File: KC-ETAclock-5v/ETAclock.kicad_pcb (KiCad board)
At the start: 2 copper layers, 240 x 38.7 mm, 125 parts, among them J1 Conn_01x01, J2 Conn_01x01, J3 Conn_01x01, J4 Conn_01x01, J5 USB_SUPPLY, J6 Conn_01x05, P15 Raspberry_PI_Zero_Hat, Q10 MMBTA42, Q11 MMBTA92, Q12 MMBTA42, Q13 MMBTA92, Q14 MMBTA42, Q15 MMBTA92, Q16 MMBTA42, Q17 MMBTA92, Q18 MMBTA42, Q19 MMBTA92, Q2 MMBTA42, Q20 MMBTA42, Q21 MMBTA92, Q22 MMBTA42, Q23 MMBTA92, Q24 MMBTA42, Q25 MMBTA92, Q3 MMBTA92, Q4 MMBTA42, Q5 MMBTA92, Q6 MMBTA42, Q7 MMBTA92, Q8 MMBTA42, Q9 MMBTA92, U10 IN-4, U11 TPIC6B595, U12 IN-4, U13 IN-4, U14 TPIC6B595, U3 IN-4, U4 TPIC6B595, U5 IN-4, U6 74HCT04, U7 TPIC6B595, U8 IN-4, U9 TPIC6B595

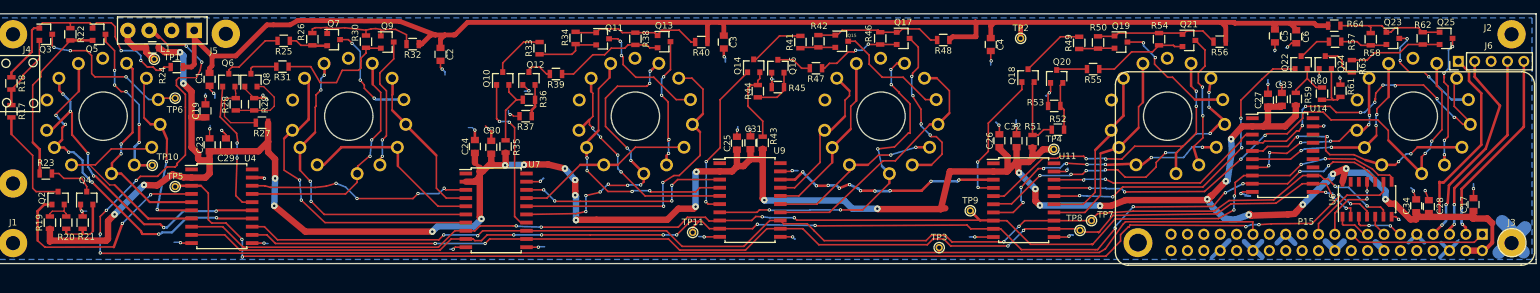
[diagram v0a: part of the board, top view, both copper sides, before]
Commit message: New V2 of Layout to Fix Nixie Tube radius offset and the Nixie tube pin 3 placement.   It is suppose to be at 49 degree C instead of 43 degree c.
Code was updated to add Fade In and Fade Out commands.  Also Code updated to
Add an option for a PIR sensor. The PIR Sensor code is working.
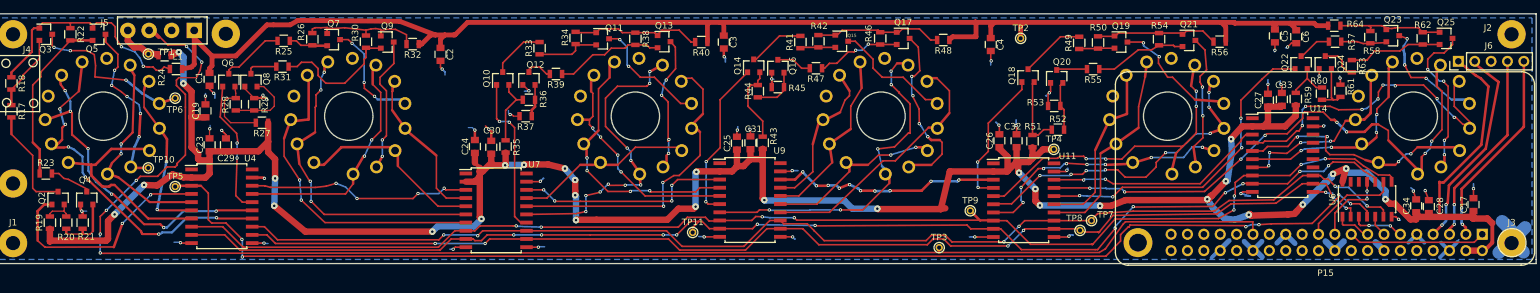
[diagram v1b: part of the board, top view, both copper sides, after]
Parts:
- moved L1 2.27 mm to (54.0, 59.1)
- moved TP1 1.22 mm to (51.5, 58.9)
- moved TP10 0.73 mm to (51.5, 76.6)
- moved Q23 0.42 mm to (244.5, 56.1)
- moved R24 0.33 mm to (55.8, 61.3)
- moved R58 0.32 mm to (241.0, 56.3)
- turned U10 to 323 degrees
- turned U12 to 323 degrees
- turned U13 to 323 degrees
- turned U3 to 323 degrees
- turned U5 to 323 degrees
- turned U8 to 323 degrees
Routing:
- net Net-(Q25-Pad3): track 21.5 -> 24.1 mm
- net Net-(Q5-Pad3): track 25.9 -> 28.1 mm
- net Net-(U3-Pad1): track 35.7 -> 37.7 mm
- net Net-(U13-Pad11): track 53.2 -> 51.5 mm
- net Net-(U11-Pad15): track 26.7 -> 28.3 mm
- net Net-(U10-Pad2): track 27.1 -> 28.7 mm
- net Net-(Q3-Pad3): track 25.9 -> 27.1 mm
- net Net-(Q9-Pad2): track 19.8 -> 21.0 mm
- net Net-(U3-Pad11): track 28.3 -> 27.1 mm
- net Net-(Q9-Pad3): track 20.7 -> 21.9 mm
- net Net-(U11-Pad17): track 86.1 -> 87.1 mm, vias 6 -> 8
- net +5V: track 436.0 -> 435.0 mm
- net Net-(Q23-Pad1): track 17.8 -> 16.8 mm
- net Net-(U3-Pad3): track 51.0 -> 50.2 mm
- net Net-(Q17-Pad3): track 26.6 -> 27.3 mm
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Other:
- board text added: "ETA_NIXIE_CLOCK_REV2_1810"
- board text removed: "ETA_NIXIE_CLOCK_REV1_1808"

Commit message: New Layout changes.  Fixed the BJT packages.  Added 1k to the 160v_enable pin to protect the rasberry pi.  Improved the 160v spacing to the power supply input.
updated the code with both a testscript and a testETAclock.py to help test the code.
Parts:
- added R90: 1k, Resistors_SMD:R_0805, F.Cu at (56.3, 70.4)
- Q11, Q13, Q15, Q17, Q19, Q21, Q23, Q25, Q3, Q5, Q7, Q9: value MMBTA92 -> MMBT3906
- moved R36 5.10 mm to (105.4, 66.8), turned to 270 degrees
- moved R28 2.03 mm to (63.0, 66.7)
- moved R37 1.89 mm to (109.5, 66.7), turned to 270 degrees
- moved R44 1.55 mm to (144.5, 65.0)
- moved R45 1.34 mm to (148.1, 65.0), turned to 270 degrees
- moved R21 1.27 mm to (42.5, 85.1)
- moved R41 0.80 mm to (151.8, 57.1)
- moved R38 0.78 mm to (127.8, 56.4), turned to 90 degrees
- moved R20 0.51 mm to (38.7, 85.6)
- moved R26 0.48 mm to (76.4, 56.7), turned to 90 degrees
- moved R34 0.24 mm to (117.7, 56.7), turned to 90 degrees
- moved L1 0.23 mm to (54.1, 58.9)
- moved TP1 0.17 mm to (51.6, 58.8)
- turned R30 to 90 degrees
- turned R42 to 90 degrees
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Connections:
- J5 pad 3: N_ENABLE_160V -> Net-(J5-Pad3)
- Q12 pad 1: GND -> Net-(Q12-Pad1)
- Q12 pad 2: Net-(Q12-Pad2) -> GND
- Q13 pad 1: Net-(Q11-Pad1) -> Net-(Q13-Pad1)
- Q13 pad 2: Net-(Q13-Pad2) -> Net-(Q11-Pad2)
- Q16 pad 1: GND -> Net-(Q16-Pad1)
- Q16 pad 2: Net-(Q16-Pad2) -> GND
- Q17 pad 1: Net-(Q15-Pad1) -> Net-(Q17-Pad1)
- Q17 pad 2: Net-(Q17-Pad2) -> Net-(Q15-Pad2)
- Q20 pad 1: GND -> Net-(Q20-Pad1)
- Q20 pad 2: Net-(Q20-Pad2) -> GND
- Q21 pad 1: Net-(Q19-Pad1) -> Net-(Q21-Pad1)
- Q21 pad 2: Net-(Q21-Pad2) -> Net-(Q19-Pad2)
- Q24 pad 1: GND -> Net-(Q24-Pad1)
- Q24 pad 2: Net-(Q24-Pad2) -> GND
- Q25 pad 1: Net-(Q23-Pad1) -> Net-(Q25-Pad1)
- Q25 pad 2: Net-(Q25-Pad2) -> Net-(Q23-Pad2)
- Q4 pad 1: GND -> Net-(Q4-Pad1)
- Q4 pad 2: Net-(Q4-Pad2) -> GND
- Q5 pad 1: Net-(Q3-Pad1) -> Net-(Q5-Pad1)
- Q5 pad 2: Net-(Q5-Pad2) -> Net-(Q3-Pad2)
- Q8 pad 1: GND -> Net-(Q8-Pad1)
- Q8 pad 2: Net-(Q8-Pad2) -> GND
- Q9 pad 1: Net-(Q7-Pad1) -> Net-(Q9-Pad1)
- Q9 pad 2: Net-(Q9-Pad2) -> Net-(Q7-Pad2)
- R17 pad 1: Net-(Q3-Pad2) -> Net-(Q3-Pad1)
- R18 pad 1: Net-(Q3-Pad1) -> Net-(Q3-Pad2)
- R18 pad 2: Net-(Q3-Pad2) -> Net-(Q3-Pad1)
- R19 pad 2: Net-(Q2-Pad2) -> Net-(Q2-Pad1)
- R20 pad 1: Net-(Q2-Pad2) -> Net-(Q2-Pad1)
- R20 pad 2: Net-(Q4-Pad2) -> Net-(Q4-Pad1)
- R21 pad 1: Net-(Q4-Pad2) -> Net-(Q4-Pad1)
- R22 pad 1: Net-(Q3-Pad1) -> Net-(Q3-Pad2)
- R22 pad 2: Net-(Q5-Pad2) -> Net-(Q5-Pad1)
- R23 pad 1: Net-(Q5-Pad2) -> Net-(Q5-Pad1)
- R24 pad 2: Net-(Q3-Pad1) -> Net-(Q3-Pad2)
- R25 pad 1: Net-(Q7-Pad2) -> Net-(Q7-Pad1)
- R26 pad 1: Net-(Q7-Pad1) -> Net-(Q7-Pad2)
- R26 pad 2: Net-(Q7-Pad2) -> Net-(Q7-Pad1)
- R27 pad 2: Net-(Q6-Pad2) -> Net-(Q6-Pad1)
- R28 pad 1: Net-(Q6-Pad2) -> Net-(Q6-Pad1)
- R28 pad 2: Net-(Q8-Pad2) -> Net-(Q8-Pad1)
- R29 pad 1: Net-(Q8-Pad2) -> Net-(Q8-Pad1)
- R30 pad 1: Net-(Q7-Pad1) -> Net-(Q7-Pad2)
- R30 pad 2: Net-(Q9-Pad2) -> Net-(Q9-Pad1)
- R31 pad 1: Net-(Q9-Pad2) -> Net-(Q9-Pad1)
- R32 pad 2: Net-(Q7-Pad1) -> Net-(Q7-Pad2)
- R33 pad 1: Net-(Q11-Pad2) -> Net-(Q11-Pad1)
- R34 pad 1: Net-(Q11-Pad1) -> Net-(Q11-Pad2)
- R34 pad 2: Net-(Q11-Pad2) -> Net-(Q11-Pad1)
- R35 pad 2: Net-(Q10-Pad2) -> Net-(Q10-Pad1)
- R36 pad 1: Net-(Q10-Pad2) -> Net-(Q10-Pad1)
- R36 pad 2: Net-(Q12-Pad2) -> Net-(Q12-Pad1)
- R37 pad 1: Net-(Q12-Pad2) -> Net-(Q12-Pad1)
- R38 pad 1: Net-(Q11-Pad1) -> Net-(Q11-Pad2)
- R38 pad 2: Net-(Q13-Pad2) -> Net-(Q13-Pad1)
- R39 pad 1: Net-(Q13-Pad2) -> Net-(Q13-Pad1)
- R40 pad 2: Net-(Q11-Pad1) -> Net-(Q11-Pad2)
- R41 pad 1: Net-(Q15-Pad2) -> Net-(Q15-Pad1)
- R42 pad 1: Net-(Q15-Pad1) -> Net-(Q15-Pad2)
- R42 pad 2: Net-(Q15-Pad2) -> Net-(Q15-Pad1)
- R43 pad 2: Net-(Q14-Pad2) -> Net-(Q14-Pad1)
- R44 pad 1: Net-(Q14-Pad2) -> Net-(Q14-Pad1)
- R44 pad 2: Net-(Q16-Pad2) -> Net-(Q16-Pad1)
- R45 pad 1: Net-(Q16-Pad2) -> Net-(Q16-Pad1)
- R46 pad 1: Net-(Q15-Pad1) -> Net-(Q15-Pad2)
- R46 pad 2: Net-(Q17-Pad2) -> Net-(Q17-Pad1)
- R47 pad 1: Net-(Q17-Pad2) -> Net-(Q17-Pad1)
- R48 pad 2: Net-(Q15-Pad1) -> Net-(Q15-Pad2)
- R49 pad 1: Net-(Q19-Pad2) -> Net-(Q19-Pad1)
- R50 pad 1: Net-(Q19-Pad1) -> Net-(Q19-Pad2)
- R50 pad 2: Net-(Q19-Pad2) -> Net-(Q19-Pad1)
- R51 pad 2: Net-(Q18-Pad2) -> Net-(Q18-Pad1)
- R52 pad 1: Net-(Q18-Pad2) -> Net-(Q18-Pad1)
- R52 pad 2: Net-(Q20-Pad2) -> Net-(Q20-Pad1)
- R53 pad 1: Net-(Q20-Pad2) -> Net-(Q20-Pad1)
- R54 pad 1: Net-(Q19-Pad1) -> Net-(Q19-Pad2)
- R54 pad 2: Net-(Q21-Pad2) -> Net-(Q21-Pad1)
- R55 pad 1: Net-(Q21-Pad2) -> Net-(Q21-Pad1)
- R56 pad 2: Net-(Q19-Pad1) -> Net-(Q19-Pad2)
- R57 pad 1: Net-(Q23-Pad2) -> Net-(Q23-Pad1)
- R58 pad 1: Net-(Q23-Pad1) -> Net-(Q23-Pad2)
- R58 pad 2: Net-(Q23-Pad2) -> Net-(Q23-Pad1)
- R59 pad 2: Net-(Q22-Pad2) -> Net-(Q22-Pad1)
- R60 pad 1: Net-(Q22-Pad2) -> Net-(Q22-Pad1)
- R60 pad 2: Net-(Q24-Pad2) -> Net-(Q24-Pad1)
- R61 pad 1: Net-(Q24-Pad2) -> Net-(Q24-Pad1)
- R62 pad 1: Net-(Q23-Pad1) -> Net-(Q23-Pad2)
- R62 pad 2: Net-(Q25-Pad2) -> Net-(Q25-Pad1)
- R63 pad 1: Net-(Q25-Pad2) -> Net-(Q25-Pad1)
- R64 pad 2: Net-(Q23-Pad1) -> Net-(Q23-Pad2)
- U11 pad 16: Net-(Q22-Pad1) -> Net-(Q22-Pad2)
- U11 pad 4: Net-(Q18-Pad1) -> Net-(Q18-Pad2)
- U4 pad 16: Net-(Q6-Pad1) -> Net-(Q6-Pad2)
- U4 pad 4: Net-(Q2-Pad1) -> Net-(Q2-Pad2)
- U7 pad 14: Net-(Q10-Pad1) -> Net-(Q10-Pad2)
- U9 pad 6: Net-(Q14-Pad1) -> Net-(Q14-Pad2)
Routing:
- net Net-(Q22-Pad2): track 7.30 -> 53.1 mm, vias 0 -> 6
- net Net-(Q22-Pad1): track 50.1 -> 8.16 mm, vias 4 -> 0
- net Net-(Q2-Pad1): track 36.0 -> 4.74 mm, vias 2 -> 0
- net Net-(Q5-Pad1): track 0.00 -> 29.6 mm, vias 0 -> 2
- net Net-(Q5-Pad2): track 26.9 -> 0.00 mm
- net Net-(Q2-Pad2): track 4.82 -> 31.5 mm, vias 0 -> 4
- net N_ENABLE_160V: track 235.4 -> 210.5 mm, vias 6 -> 4
- net Net-(Q3-Pad2): track 11.8 -> 35.3 mm, vias 0 -> 4
- net Net-(Q9-Pad1): track 0.00 -> 22.7 mm, vias 0 -> 2
- net Net-(Q9-Pad2): track 21.0 -> 0.00 mm
- net Net-(Q3-Pad1): track 37.3 -> 17.0 mm
- net Net-(Q13-Pad1): track 0.00 -> 19.1 mm, vias 0 -> 2
- net Net-(J5-Pad3): track 0.00 -> 18.3 mm, vias 0 -> 2
- net Net-(Q21-Pad1): track 0.00 -> 17.7 mm, vias 0 -> 2
- net Net-(Q25-Pad1): track 0.00 -> 16.9 mm, vias 0 -> 2
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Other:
- board text added: "+5v"
- board text added: "DANGER HIGH VOLTAGE"
- board text added: "GND"
- board text added: "GPIO02"
- board text added: "GPIO03"
- board text added: "GPIO04"

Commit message: latest
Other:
- board text added: "ETA_NIXIE_CLOCK_REV2_1812"
- board text removed: "ETA_NIXIE_CLOCK_REV2_1810"
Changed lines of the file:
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@@
     (links 314)
     (no_connects 0)
-    (area 26.594999 52.629999 266.775001 91.515001)
+    (area 12.799287 28.415 280.490715 177.128)
     (thickness 1.6)
     (drawings 32)
@@
     (effects (font (size 1 1.5) (thickness 0.2)) (justify mirror))
   )
-  (gr_text ETA_NIXIE_CLOCK_REV2_1810 (at 104.775 88.011) (layer B.SilkS)
+  (gr_text ETA_NIXIE_CLOCK_REV2_1812 (at 104.775 88.011) (layer B.SilkS)
     (effects (font (size 1 1.5) (thickness 0.25)) (justify mirror))
   )
